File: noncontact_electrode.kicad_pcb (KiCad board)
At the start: 4 copper layers, 26 x 26 mm, 10 parts, among them J1 CONN_01, J2 CONN_01, J3 CONN_01, J4 CONN_01, U1 LMP7702MM

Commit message: low impedance verison complete
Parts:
- removed C2: C, Capacitor_SMD:C_0402_1005Metric
- added R4: R, Resistor_SMD:R_0402_1005Metric, F.Cu at (102.1, 103.7)
- U1: value LMP7702MM -> LMP7721MA
- moved Gnd1 8.87 mm to (105.3, 99.2)
- moved Vcc1 7.61 mm to (94.4, 100.1)
- moved R3 7.06 mm to (99.8, 104.4), turned to 0 degrees
- moved R2 6.60 mm to (97.8, 103.7)
- moved R1 5.18 mm to (99.7, 96.3), turned to 180 degrees
- moved C1 4.91 mm to (99.7, 103.3), turned to 180 degrees
- moved Vcc/2 3.31 mm to (105.3, 101.7)
- moved Out1 1.65 mm to (105.3, 97.4)
- moved U1 0.36 mm to (99.7, 99.8), turned to 180 degrees
- renumbered J4 to Gnd1, J2 to Out1, J1 to Vcc/2, J3 to Vcc1
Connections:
- C1 pad 2: (no net) -> Net-(C1-Pad2)
- Out1 pad 1: Net-(J2-Pad1) -> Net-(C1-Pad1)
- R1 pad 1: Net-(C2-Pad2) -> Net-(C1-Pad1)
- R2 pad 1: Net-(C2-Pad1) -> Net-(C1-Pad2)
- R2 pad 2: Net-(J1-Pad1) -> Net-(R2-Pad2)
- R3 pad 1: Net-(J2-Pad1) -> Net-(R2-Pad2)
- R3 pad 2: Net-(R3-Pad2) -> Net-(C1-Pad1)
- U1 pad 1: Net-(C2-Pad2) -> Net-(R4-Pad2)
- U1 pad 2: Net-(C2-Pad2) -> (no net)
- U1 pad 3: Net-(C1-Pad1) -> GND
- U1 pad 4: GND -> Net-(C1-Pad1)
- U1 pad 5: Net-(C2-Pad1) -> (no net)
- U1 pad 6: Net-(R3-Pad2) -> VDD
- U1 pad 7: Net-(R3-Pad2) -> (no net)
- U1 pad 8: VDD -> Net-(C1-Pad2)
- Vcc/2 pad 1: Net-(J1-Pad1) -> Net-(R4-Pad2)
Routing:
- net Net-(C1-Pad1): track 2.24 -> 13.8 mm
- net Net-(C2-Pad1): track 9.02 -> 0.00 mm
- net Net-(C2-Pad2): track 5.51 -> 0.00 mm
- net (no net): track 0.00 -> 5.35 mm, vias 52 -> 51
- net Net-(C1-Pad2): track 0.00 -> 5.18 mm, vias 0 -> 1
- net Net-(R2-Pad2): track 0.00 -> 5.08 mm
- net Net-(R4-Pad2): track 0.00 -> 4.67 mm
- net Net-(R3-Pad2): track 3.13 -> 0.00 mm
- net Net-(J1-Pad1): track 2.00 -> 0.00 mm
- net Net-(J2-Pad1): track 1.88 -> 0.00 mm
- net GND: track 1.55 -> 3.12 mm
- net VDD: track 1.89 -> 3.24 mm

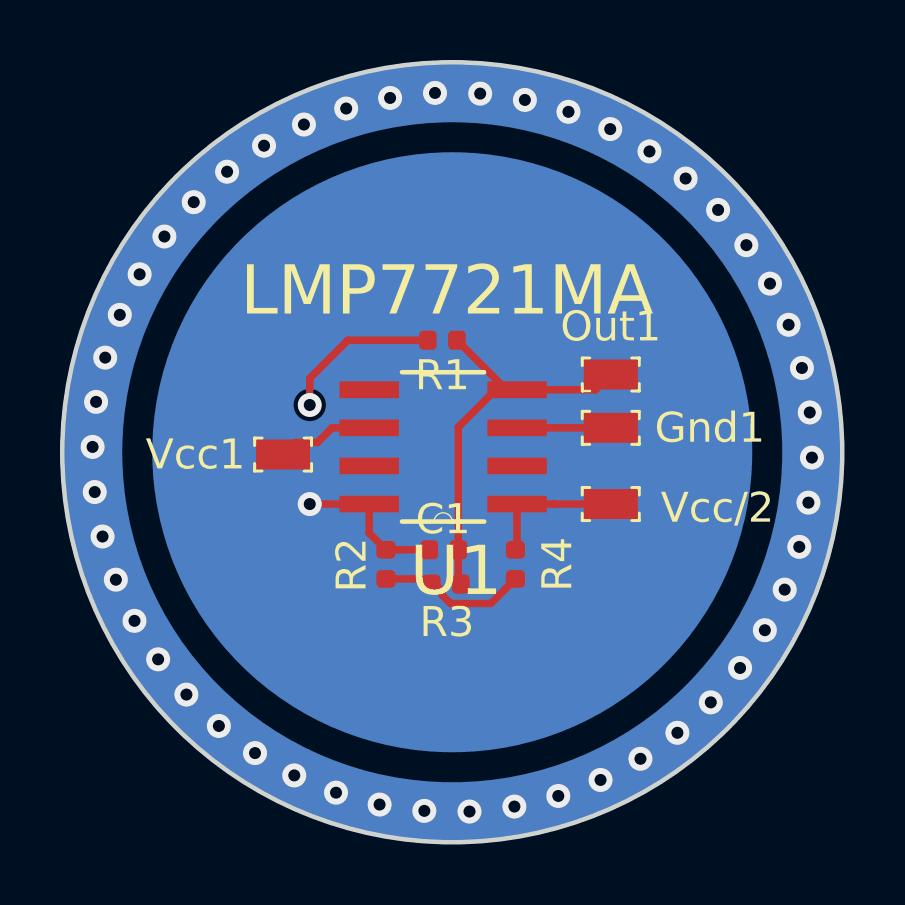
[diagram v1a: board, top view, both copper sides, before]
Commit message: high impedance done
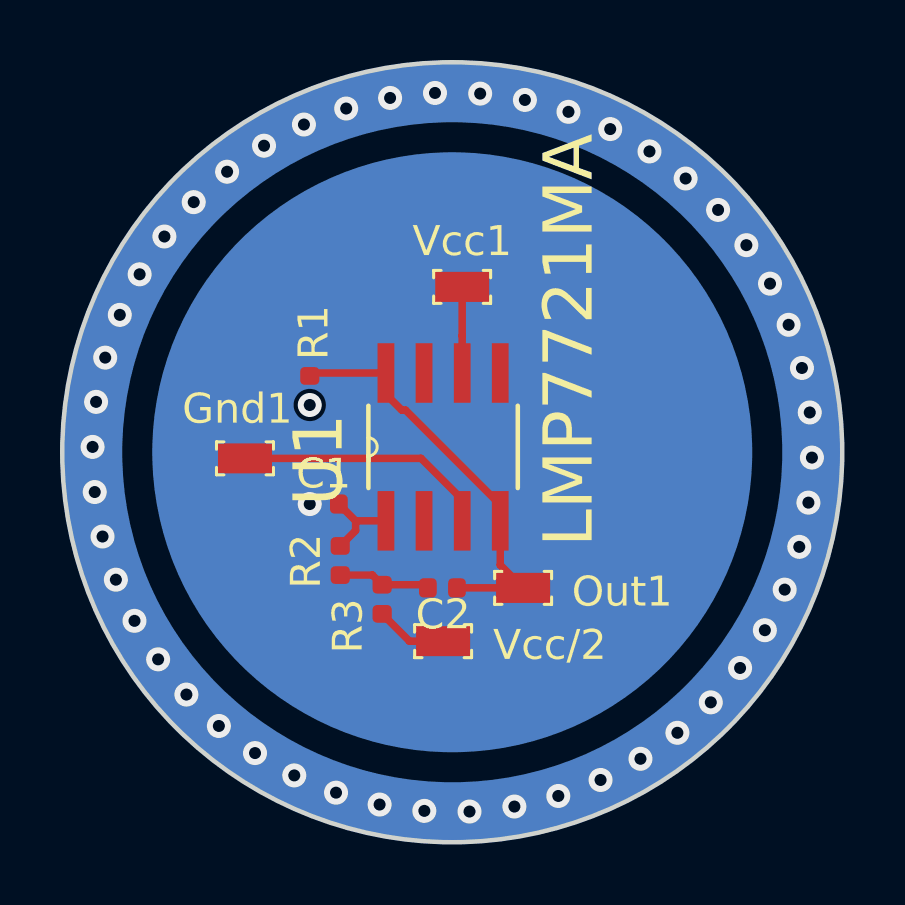
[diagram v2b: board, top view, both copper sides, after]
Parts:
- removed R4: R, Resistor_SMD:R_0402_1005Metric
- added C2: C, Capacitor_SMD:C_0402_1005Metric, F.Cu at (99.7, 104.5)
- moved Gnd1 12.2 mm to (93.1, 100.2)
- moved Vcc1 8.18 mm to (100.3, 94.5)
- moved Out1 7.69 mm to (102.4, 104.5)
- moved Vcc/2 7.22 mm to (99.7, 106.3)
- moved R1 4.73 mm to (95.2, 97.9), turned to 270 degrees
- moved C1 4.26 mm to (95.7, 101.7)
- moved R3 2.20 mm to (97.7, 104.9), turned to 270 degrees
- moved R2 1.53 mm to (96.3, 103.6)
- turned U1 to 90 degrees
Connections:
- C1 pad 2: Net-(C1-Pad2) -> (no net)
- Out1 pad 1: Net-(C1-Pad1) -> Net-(C2-Pad2)
- R1 pad 1: Net-(C1-Pad1) -> Net-(C2-Pad2)
- R2 pad 1: Net-(C1-Pad2) -> Net-(C1-Pad1)
- R3 pad 2: Net-(C1-Pad1) -> Net-(R3-Pad2)
- U1 pad 1: Net-(R4-Pad2) -> Net-(C1-Pad1)
- U1 pad 4: Net-(C1-Pad1) -> Net-(C2-Pad2)
- U1 pad 8: Net-(C1-Pad2) -> Net-(C2-Pad2)
- Vcc/2 pad 1: Net-(R4-Pad2) -> Net-(R3-Pad2)
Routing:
- net Net-(C2-Pad2): track 0.00 -> 13.9 mm
- net Net-(C1-Pad1): track 13.8 -> 2.85 mm
- net GND: track 3.12 -> 8.52 mm
- net (no net): track 5.35 -> 0.00 mm, vias 51 -> 52
- net Net-(C1-Pad2): track 5.18 -> 0.00 mm, vias 1 -> 0
- net Net-(R4-Pad2): track 4.67 -> 0.00 mm
- net Net-(R3-Pad2): track 0.00 -> 2.41 mm
- net Net-(C2-Pad1): track 5.08 -> 3.10 mm

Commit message: might've forgotten to commit
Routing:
- net (no net): vias 52 -> 51
- added copper zone on F.Cu, net (none)
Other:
- copper layers 4 -> 2
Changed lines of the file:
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@@
     (thickness 1.6)
     (drawings 9)
-    (tracks 77)
+    (tracks 76)
     (zones 0)
     (modules 10)
@@
   (layers
     (0 F.Cu signal)
-    (1 In1.Cu signal)
-    (2 In2.Cu signal)
     (31 B.Cu signal)
     (32 B.Adhes user)
@@
     (add_net "Net-(C2-Pad2)")
     (add_net "Net-(R3-Pad2)")
-    (add_net "Net-(U1-Pad2)")
-    (add_net "Net-(U1-Pad5)")
-    (add_net "Net-(U1-Pad7)")
     (add_net VDD)
   )
@@
     )
   )
+  (gr_poly (pts (xy 94.361 98.044) (xy 96.266 98.044) (xy 96.393 99.06) (xy 95.631 99.314) (xy 94.488 99.314) (xy 94.107 98.552)) (layer F.Cu) (width 0.1))
+  (gr_circle (center 100 100) (end 111 100) (layer F.Cu) (width 4))
+  (gr_circle (center 100 100) (end 113 100) (layer Edge.Cuts) (width 0.05))
+  (gr_poly (pts (xy 94.107 97.409) (xy 96.901 97.536) (xy 96.393 99.568) (xy 94.234 99.568)) (layer B.Cu) (width 0.1))
   (gr_circle (center 100 100) (end 113 100) (layer B.Mask) (width 0.15))
-  (gr_circle (center 100 100) (end 113 100) (layer Edge.Cuts) (width 0.15))
-  (gr_poly (pts (xy 90.932 93.345) (xy 97.917 89.154) (xy 106.807 91.567) (xy 111.252 100.076) (xy 104.775 110.744) (xy 97.282 110.617) (xy 90.932 105.664) (xy 92.71 103.378) (xy 96.774 102.489) (xy 94.742 99.949) (xy 88.9 101.727)) (layer In1.Cu) (width 0.1))
-  (gr_circle (center 100 100) (end 111 100) (layer In1.Cu) (width 4))
-  (gr_circle (center 95.25 101.727) (end 97.788815 101.727) (layer In1.Cu) (width 4.12))
   (gr_poly (pts (xy 93.345 100.33) (xy 92.964 104.394) (xy 98.171 108.966) (xy 106.299 106.426) (xy 108.077 102.489) (xy 107.696 97.155) (xy 104.648 92.964) (xy 98.044 91.821) (xy 94.361 93.726) (xy 97.155 98.679)) (layer B.Cu) (width 0.1))
   (gr_circle (center 100 100) (end 108.5 100) (layer B.Cu) (width 3))
   (gr_circle (center 95.25 98.425) (end 97.788815 98.425) (layer B.Cu) (width 4))
   (gr_circle (center 100 100) (end 112 100) (layer B.Cu) (width 2))
-  (via (at 95.25 98.425) (size 0.8) (drill 0.4) (layers F.Cu B.Cu) (net 0))
   (via (at 88.011 99.822) (size 0.8) (drill 0.4) (layers F.Cu B.Cu) (net 0))
   (via (at 88.083228 101.326024) (size 0.8) (drill 0.4) (layers F.Cu B.Cu) (net 0))
@@
   (segment (start 97.663 105.387) (end 98.575 106.299) (width 0.25) (layer F.Cu) (net 6))
   (segment (start 98.575 106.299) (end 99.695 106.299) (width 0.25) (layer F.Cu) (net 6))
-  (zone (net 0) (net_name "") (layer In1.Cu) (hatch edge 0.508)
+  (zone (net 0) (net_name "") (layer F.Cu) (hatch edge 0.508)
     (connect_pads (clearance 0.508))
     (min_thickness 0.254)
-    (keepout (tracks not_allowed) (vias not_allowed) (copperpour allowed))
-    (fill (arc_segments 32) (thermal_gap 0.508) (thermal_bridge_width 0.508))
+    (fill yes (arc_segments 32) (thermal_gap 0.508) (thermal_bridge_width 0.508))
     (polygon
       (pts
-        (xy 94.869 100.965) (xy 95.758 101.219) (xy 95.885 102.362) (xy 94.488 102.362)
+        (xy 92.456 90.043) (xy 96.774 87.63) (xy 103.759 88.265) (xy 109.728 93.218) (xy 112 100)
+        (xy 110.49 105.41) (xy 106.045 110.109) (xy 98.552 112.268) (xy 93.472 110.363) (xy 88.9 105.537)
+        (xy 87.63 98.679) (xy 90.043 92.837) (xy 92.329 90.043)
       )
     )
-  )
-  (zone (net 0) (net_name "") (layer In1.Cu) (hatch edge 0.508)
-    (connect_pads (clearance 0.508))
-    (min_thickness 0.254)
-    (keepout (tracks not_allowed) (vias not_allowed) (copperpour not_allowed))
-    (fill (arc_segments 32) (thermal_gap 0.508) (thermal_bridge_width 0.508))
-    (polygon
-      (pts
-        (xy 94.742 101.219) (xy 95.758 101.219) (xy 95.758 102.235) (xy 94.742 102.235) (xy 94.742 102.108)
-      )
-    )
